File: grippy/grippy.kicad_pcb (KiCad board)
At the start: 2 copper layers, 60.8 x 35.2 mm, 9 parts, among them J1 Conn_01x08_Socket, SW0 SW_SPST, SW1 SW_SPST, SW2 SW_SPST, SW3 SW_SPST, SW4 SW_SPST, SW5 SW_DPDT_x2, U1 esp32s3-supermini

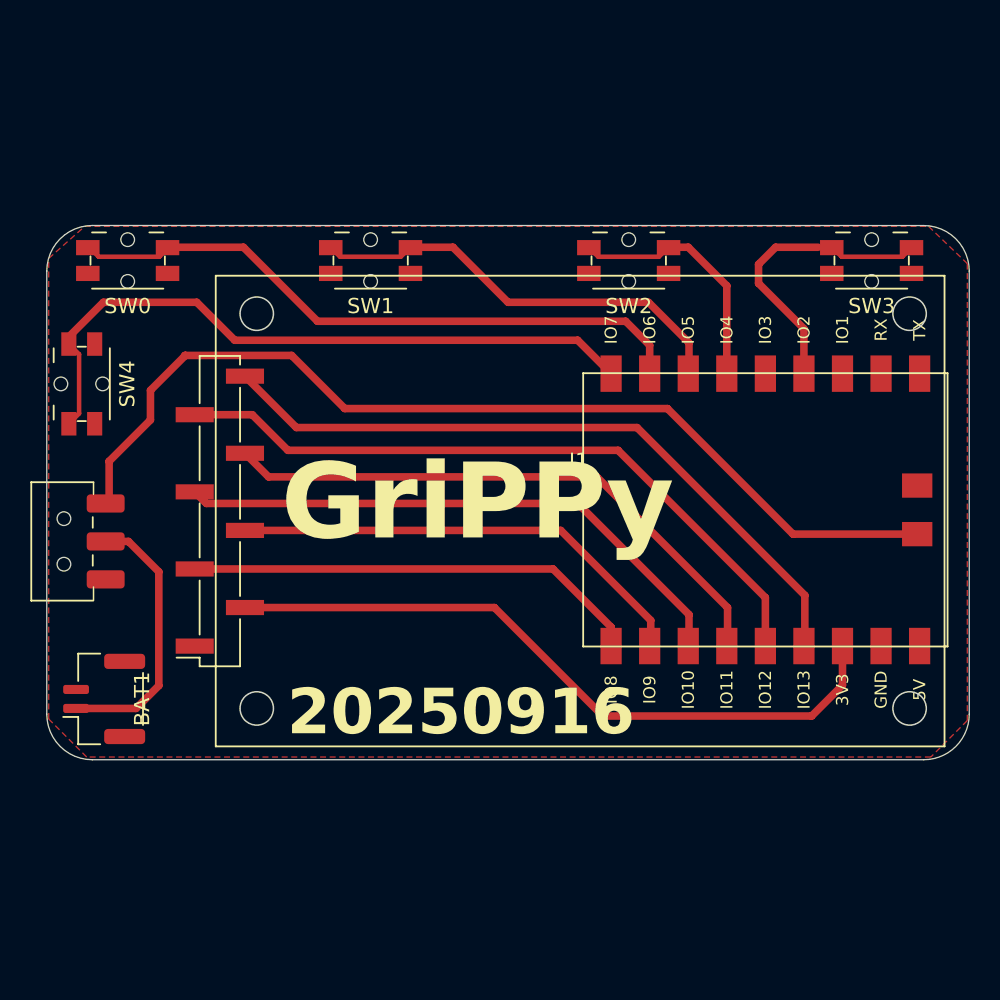
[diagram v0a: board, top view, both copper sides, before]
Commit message: kicad mods
* raised display height to 8mm
* slide thumb button
* changed tft header location 1.25mm slide toward mcu
* rotated power plug
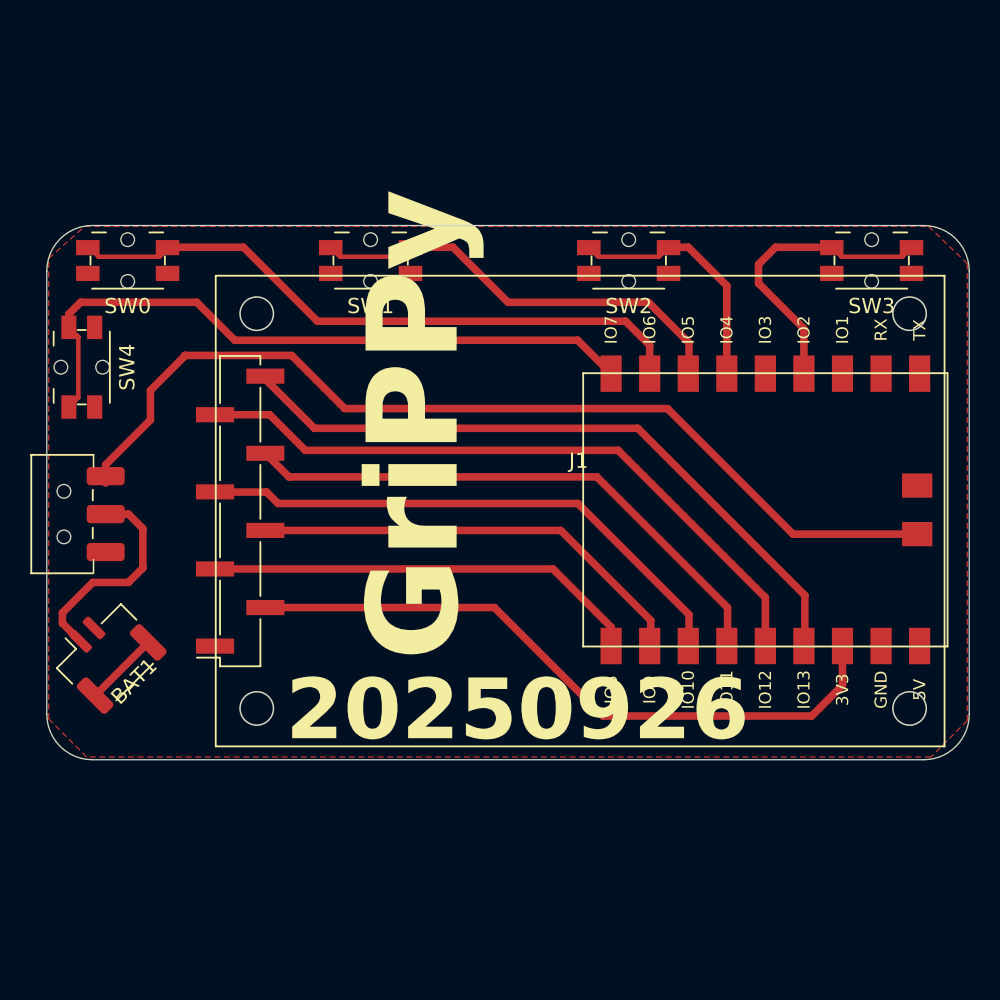
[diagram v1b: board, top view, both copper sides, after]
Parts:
- moved BAT1 2.93 mm to (180.9, 95.0), turned to 45 degrees
- moved SW5 1.80 mm to (178.2, 85.7)
- moved SW4 1.10 mm to (179.2, 76.0)
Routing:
- net /mp: track 0.00 -> 4.95 mm
- net /B+: track 17.2 -> 14.3 mm
- net /CS: track 46.5 -> 44.4 mm
- net /RAW: track 65.0 -> 63.7 mm
- net /SCL: track 30.5 -> 29.2 mm
- net /RES: track 38.3 -> 36.9 mm
- net /DC: track 38.8 -> 37.5 mm
- net VCC: track 45.7 -> 44.4 mm
- net /SDA: track 31.2 -> 29.8 mm
- net /BLK: track 46.5 -> 45.3 mm
- net /thumb: track 45.4 -> 44.3 mm
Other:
- board text added: "20250926"
- board text removed: "20250916"

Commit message: working model
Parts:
- moved SW3 41.7 mm to (220.4, 109.2), turned to -90 degrees
- moved SW0 39.2 mm to (220.4, 60.2), turned to -90 degrees
- moved SW4 39.1 mm to (213.4, 57.2), turned to 0 degrees
- moved SW5 38.9 mm to (203.8, 56.3), turned to 180 degrees
- moved BAT1 38.5 mm to (194.5, 58.9), turned to -45 degrees
- moved U1 26.3 mm to (204.0, 102.2), turned to 0 degrees
- moved SW2 24.8 mm to (220.4, 93.2), turned to -90 degrees
- moved SW1 23.4 mm to (220.4, 76.2), turned to -90 degrees
- moved J1 9.25 mm to (203.9, 90.0), turned to -90 degrees
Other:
- board size 60.8 x 35.2 mm -> 35.2 x 60.8 mm
